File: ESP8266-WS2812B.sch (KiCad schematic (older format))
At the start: 12 parts

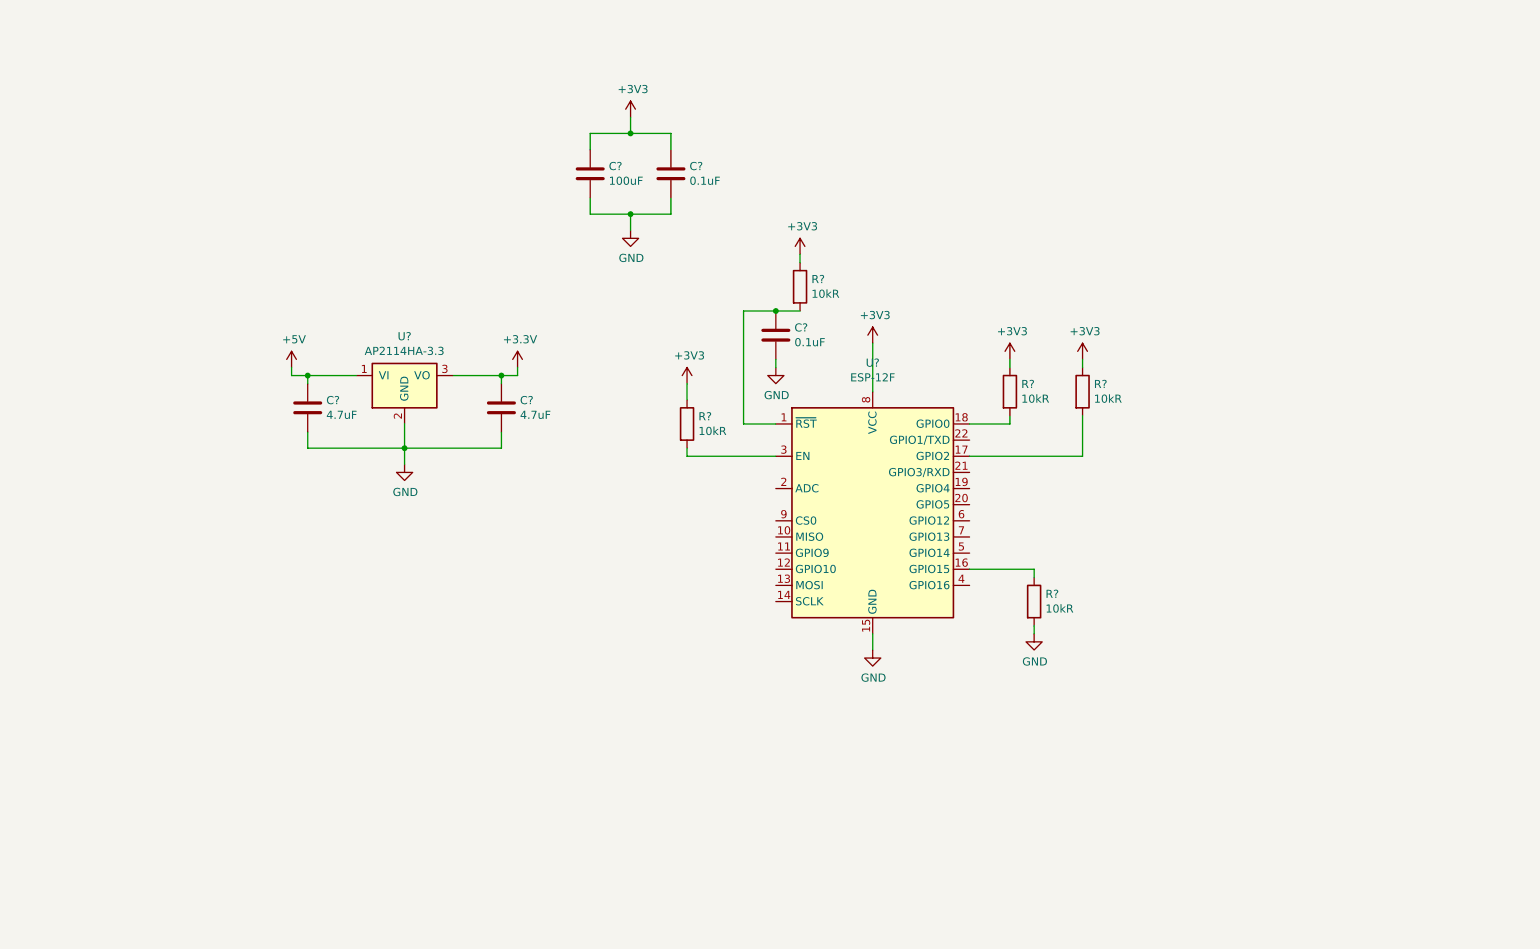
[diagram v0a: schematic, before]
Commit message: Moved the ESP8266 module and it's programming circuitry to it's own hierarchical sheet. Also added user and power LEDs.
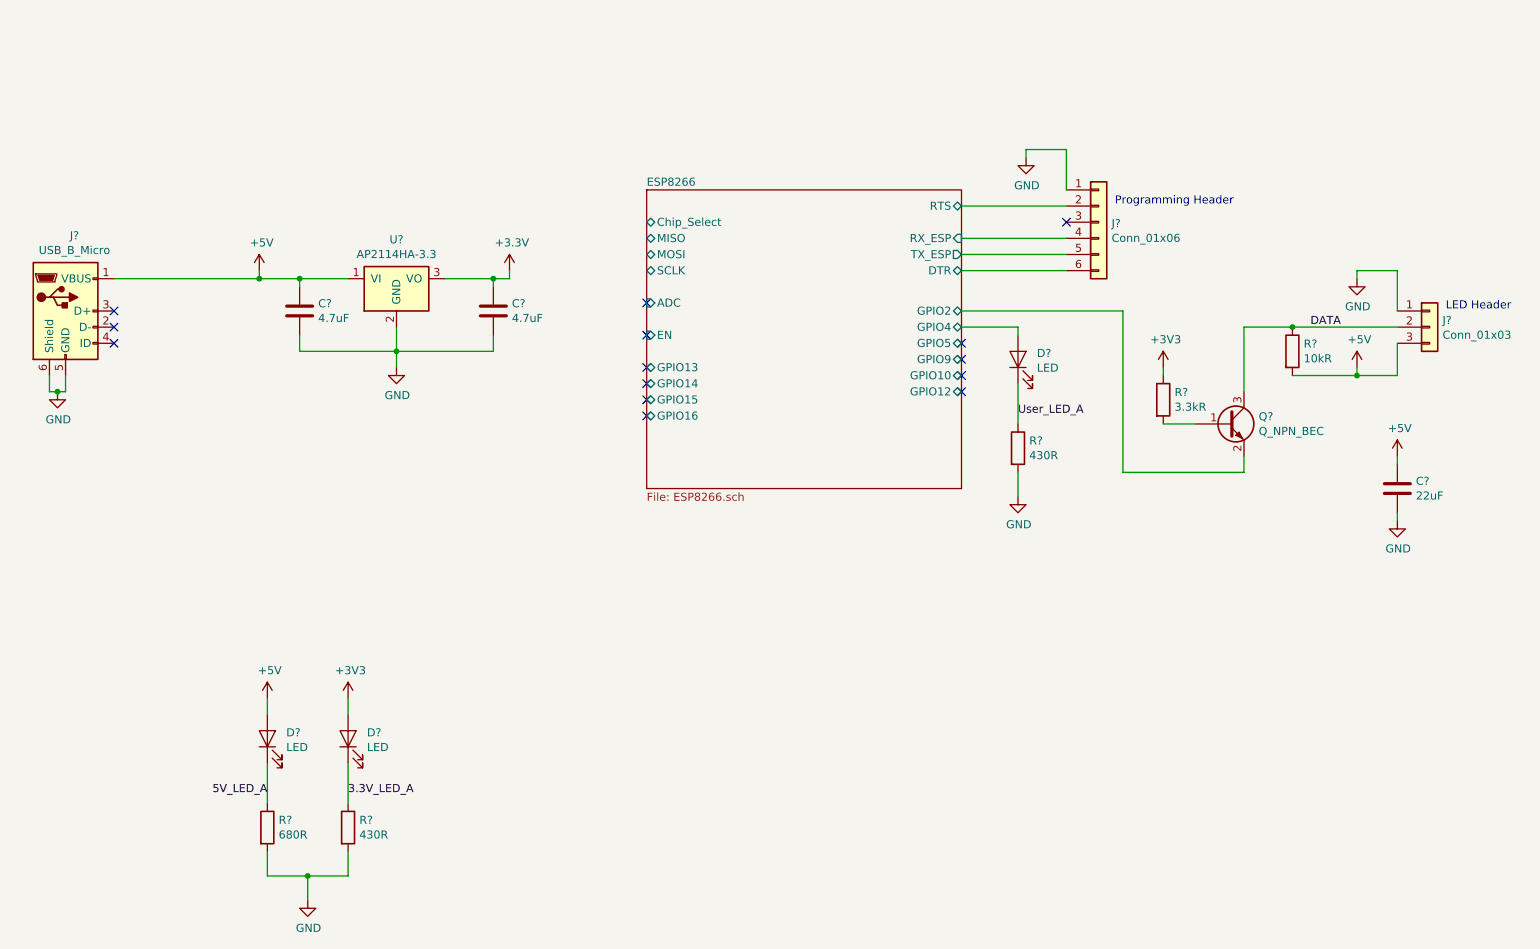
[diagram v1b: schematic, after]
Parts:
- removed C? (x2): 0.1uF, symbol Device:C
- removed C?: 100uF, symbol Device:C
- removed R? (x5): 10kR, symbol Device:R
- removed U?: ESP-12F, RF_Module:ESP-12E, symbol RF_Module:ESP-12F
- removed U?: AP2114HA-3.3, symbol 3.3V-reg:AP2114HA-3.3
- added C?: 22uF, Capacitors_THT:CP_Radial_D5.0mm_P2.50mm, symbol Device:C
- added D? (x3): LED, symbol Device:LED
- added J?: USB_B_Micro, symbol Connector:USB_B_Micro
- added J?: Conn_01x06, symbol Connector_Generic:Conn_01x06
- added J?: Conn_01x03, symbol Connector_Generic:Conn_01x03
- added Q?: Q_NPN_BEC, symbol Device:Q_NPN_BEC
- added R?: 10kR, symbol Device:R
- added R?: 3.3kR, symbol Device:R
- added R?: 680R, symbol Device:R
- added R? (x2): 430R, symbol Device:R
- added U?: AP2114HA-3.3, symbol 3.3V-reg:AP2114HA-3.3
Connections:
- net +3V3: now also D?.2 (A), R?.1, U?.3 (VO)
- net +5V: now also C?.1, D?.2 (A), J?.1 (VBUS), J?.3 (Pin_3), R?.2, U?.1 (VI)
- net GND: now also C?.2, J?.1 (Pin_1), J?.1 (Pin_1), J?.5 (GND), J?.6 (Shield), R?.2, R?.2, R?.2, U?.2 (GND), U?.4 (GND_PAD)
- new net: Q?.1 (B), R?.2
- new net 3.3V_LED_A: D?.1 (K), R?.1
- new net 5V_LED_A: D?.1 (K), R?.1
- new net DATA: J?.2 (Pin_2), Q?.3 (C), R?.1
- new net ESP8266/DTR: J?.6 (Pin_6)
- new net ESP8266/GPIO2: Q?.2 (E)
- new net ESP8266/GPIO4: D?.2 (A)
- new net ESP8266/RTS: J?.2 (Pin_2)
- new net ESP8266/RX_ESP: J?.4 (Pin_4)
- new net ESP8266/TX_ESP: J?.5 (Pin_5)
- new net User_LED_A: D?.1 (K), R?.1
- no-connect marks 0 -> 14
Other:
- note added: "LED Header"
- note added: "Programming Header"
- moved on the sheet: C?

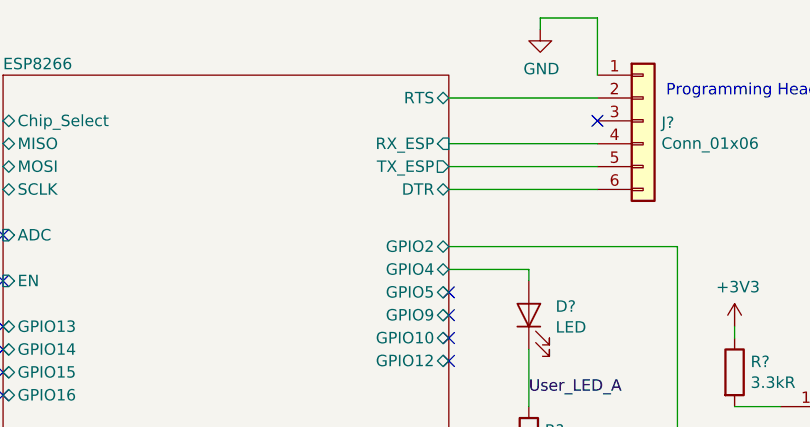
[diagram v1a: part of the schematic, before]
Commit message: Removed auto-programming circuit to conserve space, this will need it's own separate board.
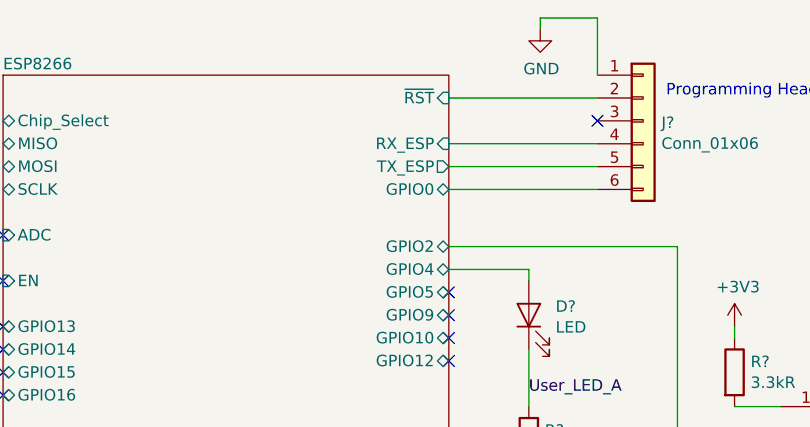
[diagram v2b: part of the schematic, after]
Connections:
- net ESP8266/DTR renamed ESP8266/GPIO0
- net ESP8266/RTS renamed ESP8266/~RST
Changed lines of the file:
@@
 F3 "RX_ESP" I R 6950 2750 50
 F4 "GPIO2" B R 6950 3200 50
-F5 "DTR" B R 6950 2950 50
-F6 "RTS" B R 6950 2550 50
-F7 "Chip_Select" B L 5000 2650 50
-F8 "MISO" B L 5000 2750 50
-F9 "MOSI" B L 5000 2850 50
-F10 "SCLK" B L 5000 2950 50
-F11 "ADC" I L 5000 3150 50
-F12 "GPIO9" T R 6950 3500 50
-F13 "GPIO10" T R 6950 3600 50
-F14 "GPIO4" T R 6950 3300 50
-F15 "GPIO5" T R 6950 3400 50
-F16 "GPIO12" T R 6950 3700 50
-F17 "GPIO13" T L 5000 3550 50
-F18 "GPIO14" T L 5000 3650 50
-F19 "GPIO16" T L 5000 3850 50
-F20 "GPIO15" T L 5000 3750 50
-F21 "EN" I L 5000 3350 50
+F5 "Chip_Select" B L 5000 2650 50
+F6 "MISO" B L 5000 2750 50
+F7 "MOSI" B L 5000 2850 50
+F8 "SCLK" B L 5000 2950 50
+F9 "ADC" I L 5000 3150 50
+F10 "GPIO9" T R 6950 3500 50
+F11 "GPIO10" T R 6950 3600 50
+F12 "GPIO4" T R 6950 3300 50
+F13 "GPIO5" T R 6950 3400 50
+F14 "GPIO12" T R 6950 3700 50
+F15 "GPIO13" T L 5000 3550 50
+F16 "GPIO14" T L 5000 3650 50
+F17 "GPIO16" T L 5000 3850 50
+F18 "GPIO15" T L 5000 3750 50
+F19 "EN" I L 5000 3350 50
+F20 "~RST" I R 6950 2550 50
+F21 "GPIO0" T R 6950 2950 50
 $EndSheet
 Wire Wire Line

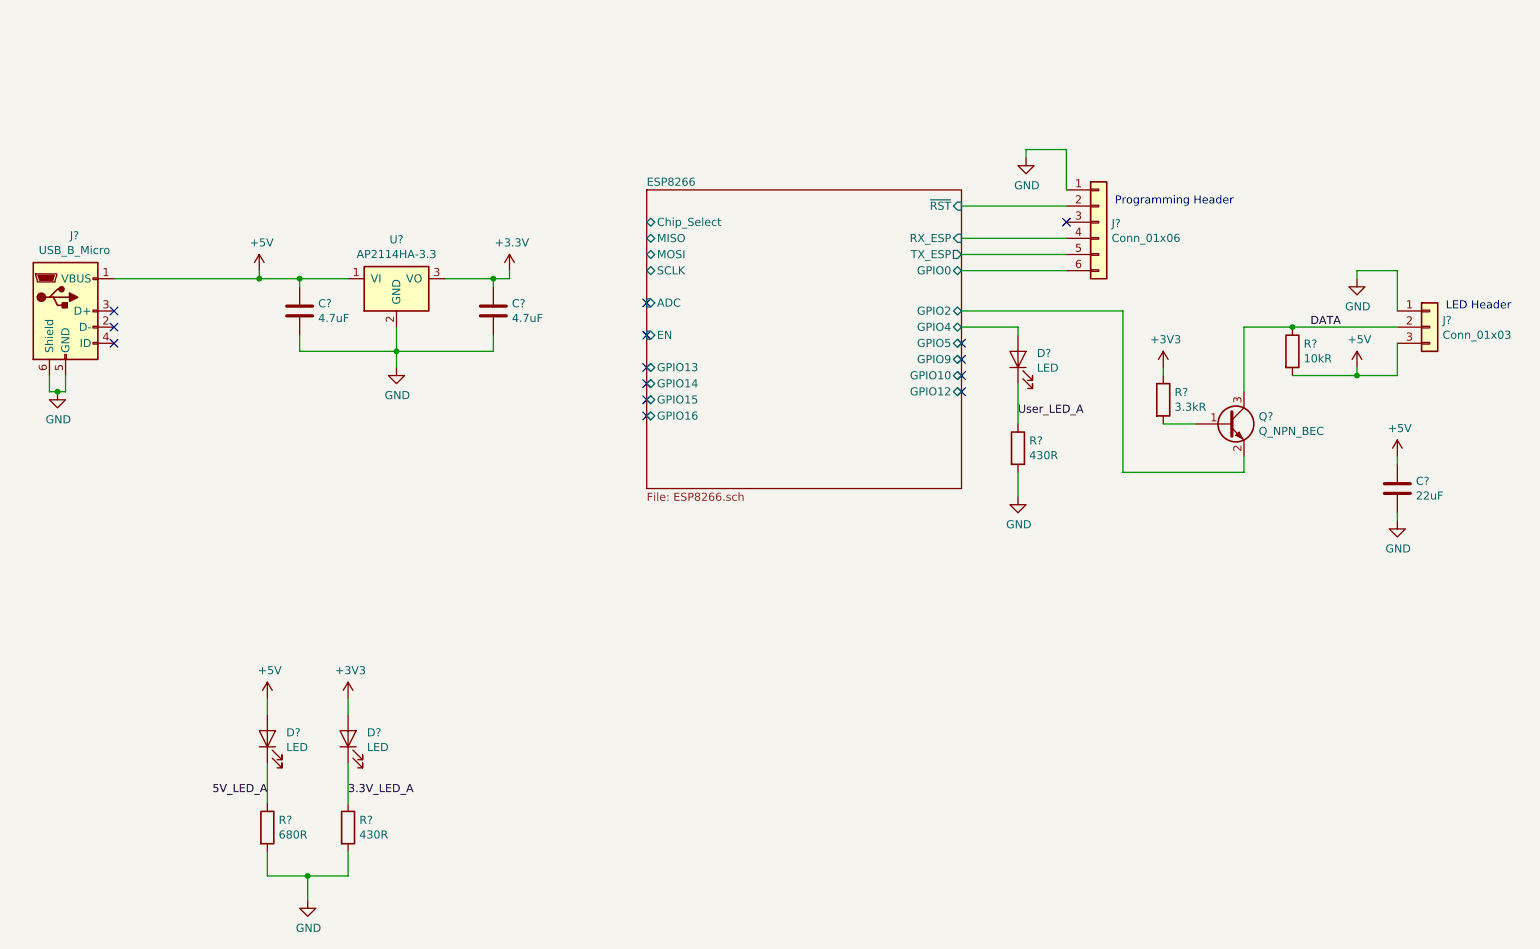
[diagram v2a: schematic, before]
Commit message: Moved 3.3V regulator to its own sheet for easier future resuse and tidied up/named some nets.
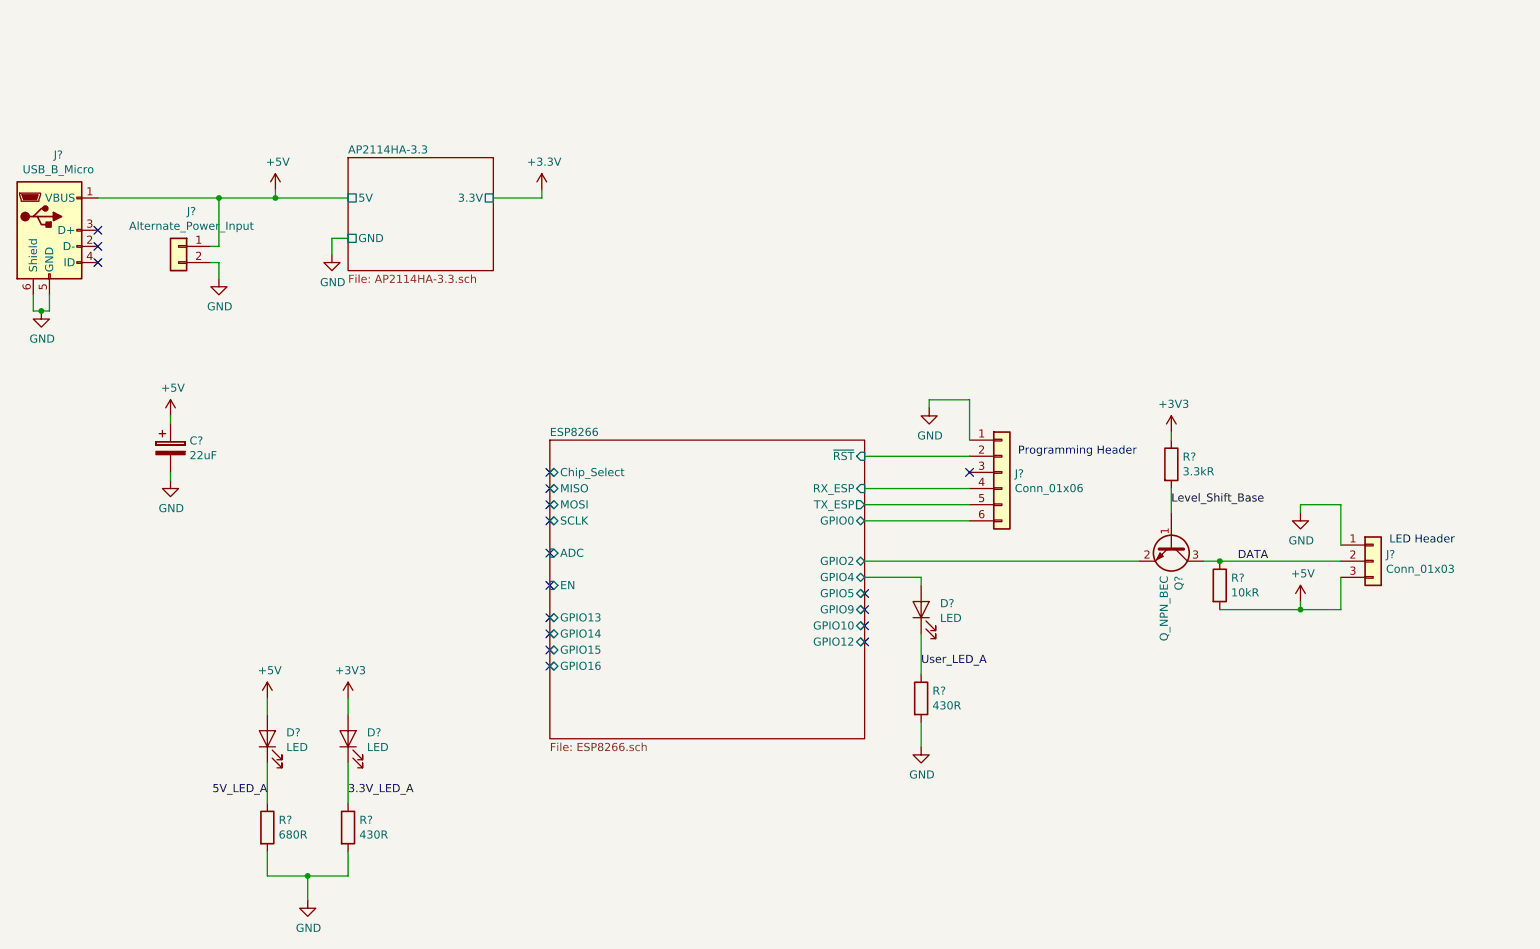
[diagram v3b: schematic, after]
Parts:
- removed C? (x2): 4.7uF, symbol Device:C
- removed C?: 22uF, Capacitors_THT:CP_Radial_D5.0mm_P2.50mm, symbol Device:C
- removed U?: AP2114HA-3.3, symbol 3.3V-reg:AP2114HA-3.3
- added C?: 22uF, symbol Device:CP
- added J?: Alternate_Power_Input, symbol Connector_Generic:Conn_01x02
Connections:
- net +5V: now also C?.1, J?.1 (Pin_1)
- net GND: now also C?.2, J?.2 (Pin_2)
- net Level_Shift_Base: now reaches Q?.1 (B), R?.2
- no-connect marks 14 -> 18
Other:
- moved on the sheet: D?, J?, Q?, R?
